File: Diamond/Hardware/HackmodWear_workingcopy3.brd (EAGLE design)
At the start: 99.9 x 104.8 mm, 127 parts, among them Q1 ZXMP6A13F, U1 ATSAMD21G-A, U2 3.3V, U5 OPA344, U6 ADMP401, U7 APDS-9960, Y1 32.768kHz

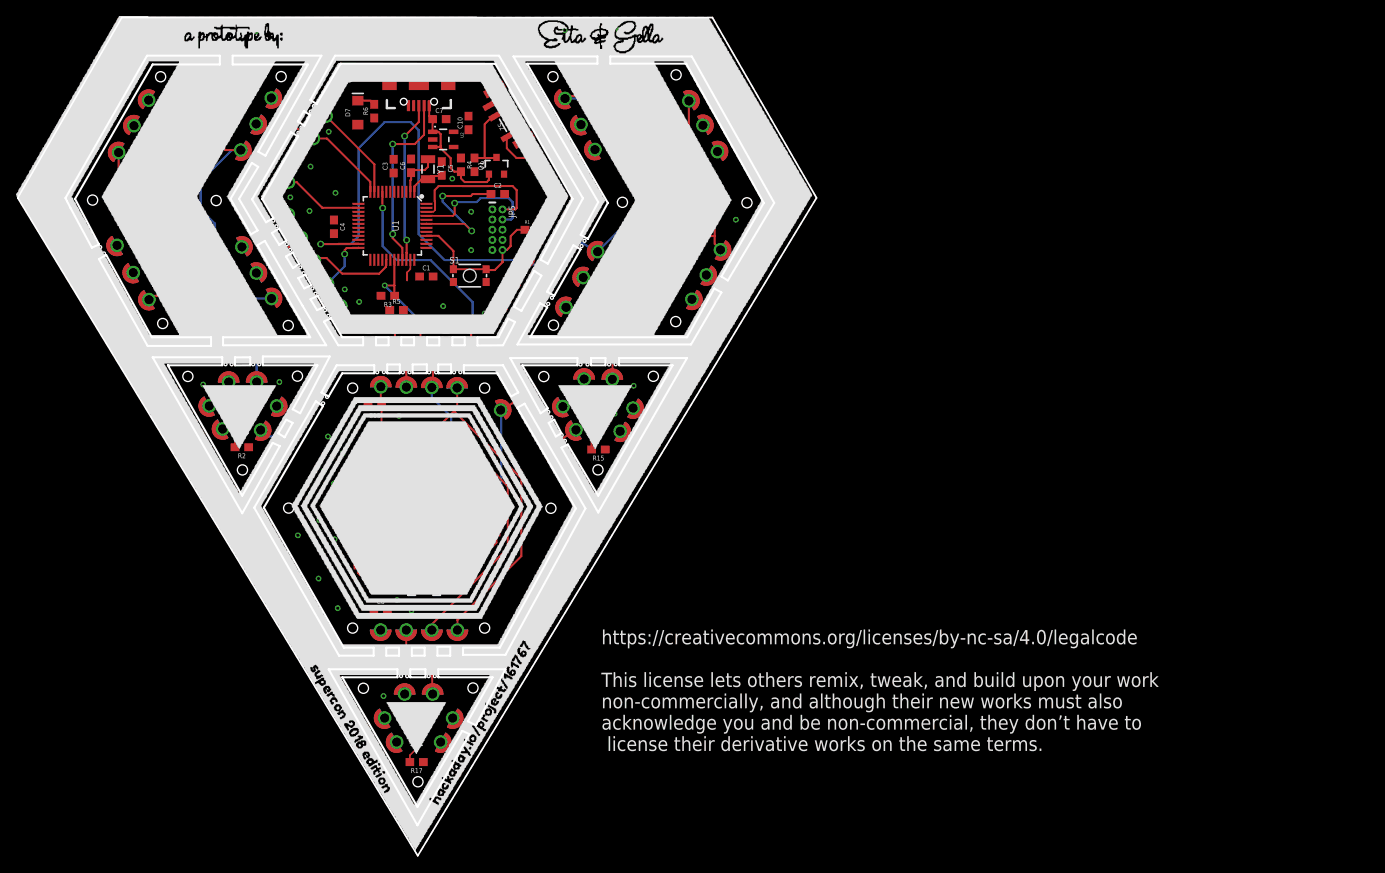
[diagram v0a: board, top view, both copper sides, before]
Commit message: Updates to power supply section
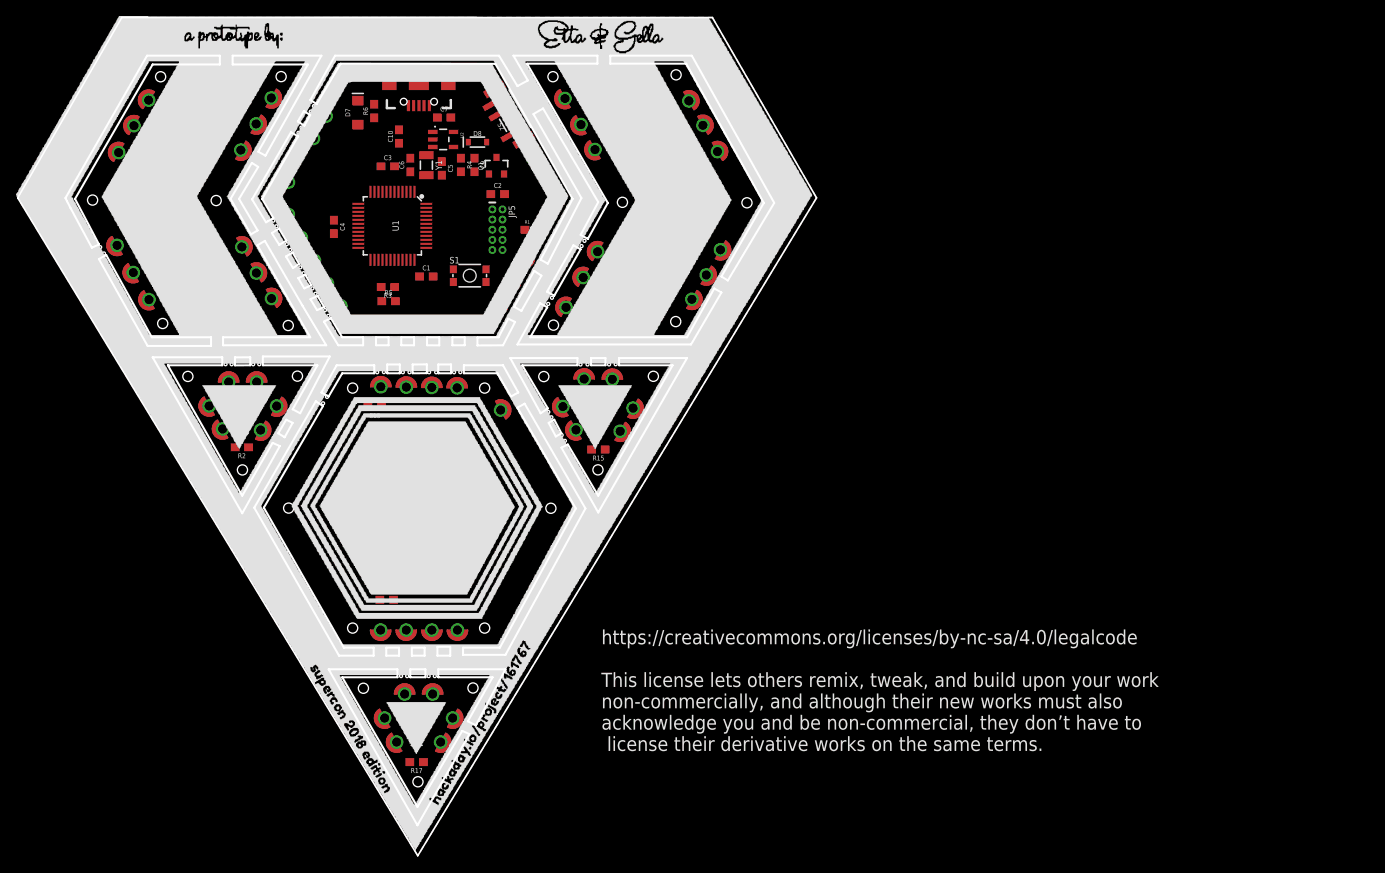
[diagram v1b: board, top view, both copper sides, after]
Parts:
- added D8: 1A/23V/620mV, SparkFun-DiscreteSemi:SOD-323
- R4: value 10k -> 100k
- moved C10 8.86 mm to (48.3, 90.7)
- moved C17 3.11 mm to (56.3, 45.3)
- moved C18 3.11 mm to (55.2, 39.8)
- moved C19 3.11 mm to (60.5, 45.2)
- moved C20 3.11 mm to (44.0, 45.7)
- moved R11 3.11 mm to (44.0, 43.9)
- moved R12 3.11 mm to (58.4, 45.2)
- moved R13 3.11 mm to (44.0, 40.2)
- moved R9 3.11 mm to (44.0, 42.0)
- moved U5 3.11 mm to (51.7, 44.4)
- moved U6 3.11 mm to (51.5, 38.0)
- moved C8 1.49 mm to (46.8, 32.8)
- moved R5 1.49 mm to (47.0, 70.1)
- moved R3 1.10 mm to (46.9, 71.9)
- moved C3 0.73 mm to (46.9, 87.0), turned to 0 degrees
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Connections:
- removed net N$21: J71.P$1, S2.3
- new net IN: C7.1, S2.2, U2.1, U2.3
- new net N$8: D8.C, Q1.2, S2.3
- net 3.3V: no longer Q1.2
- net VBUS: now also D8.A; no longer C7.1, U2.1, U2.3
- net VIN: now also J71.P$1; no longer S2.2
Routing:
- net D2: track 108.9 -> 0.00 mm, vias 3 -> 0
- net A3: track 85.0 -> 0.00 mm, vias 3 -> 0
- net SDA: track 63.5 -> 0.00 mm, vias 2 -> 0
- net D9: track 59.5 -> 0.00 mm
- net GND: track 58.1 -> 0.00 mm, vias 70 -> 0
- net SCL: track 46.7 -> 0.00 mm, vias 2 -> 0
- net DOUT: track 30.0 -> 0.00 mm
- net DO: track 25.0 -> 0.00 mm
- net N$23: track 24.9 -> 0.00 mm, vias 2 -> 0
- net USB_D-: track 23.0 -> 0.00 mm, vias 2 -> 0
- net N$11: track 22.9 -> 0.00 mm, vias 2 -> 0
- net N$6: track 21.8 -> 0.00 mm
- net USB_D+: track 20.1 -> 0.00 mm, vias 2 -> 0
- net !RESET: track 19.2 -> 0.00 mm
- net SWDIO: track 18.4 -> 0.00 mm
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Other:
- outline, holes or cut-outs redrawn
